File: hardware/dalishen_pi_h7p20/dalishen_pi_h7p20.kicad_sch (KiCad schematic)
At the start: 113 parts, among them J6 5V, J7 OV5640, J8 Conn_02x07_Odd_Even, J9 D500C930SV0, SW1 SW_Push, SW2 SW_Push, U3 H7P20N0L128-M3H1, U4 SY7201ABC, U5 XC6206-2.8, U7 P25Q32SH-SSH-IT, U8 XC6206-1.5, X2 XO32,26M

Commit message: [usb_sniffer_h7p20] 结构优化与验证
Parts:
- removed D7: 1N5819(S4),NC, vllogic:D_SOD-323_BAT60, symbol Device:D_Schottky
- removed J8: Conn_02x07_Odd_Even, Connector_PinHeader_1.27mm:PinHeader_2x07_P1.27mm_Vertical_SMD, symbol Connector_Generic:Conn_02x07_Odd_Even
- removed JP1: SolderJumper_3_Bridged12, Jumper:SolderJumper-3_P1.3mm_Bridged12_RoundedPad1.0x1.5mm_NumberLabels, symbol Jumper:SolderJumper_3_Bridged12
- removed JP7, JP8: SolderJumper_2_Bridged, Jumper:SolderJumper-2_P1.3mm_Bridged_RoundedPad1.0x1.5mm, symbol Jumper:SolderJumper_2_Bridged
- removed R12, R13, R59, R60, R7: 5.1k, Resistor_SMD:R_0402_1005Metric, symbol Device:R
- removed R14, R17, R6, R67, R8, R9: 0,NC, Resistor_SMD:R_0402_1005Metric, symbol Device:R
- removed R58: NC, Resistor_SMD:R_0402_1005Metric, symbol Device:R
- added J1: Conn_02x05_Odd_Even, Connector_PinHeader_1.27mm:PinHeader_2x05_P1.27mm_Vertical_SMD, symbol Connector_Generic:Conn_02x05_Odd_Even
- added JP1, JP10: SolderJumper_2_Open, Jumper:SolderJumper-2_P1.3mm_Open_RoundedPad1.0x1.5mm, symbol Jumper:SolderJumper_2_Open
- added SW3: SW_DIP_x03, Button_Switch_SMD:SW_DIP_SPSTx03_Slide_6.7x9.18mm_W8.61mm_P2.54mm_LowProfile, symbol Switch:SW_DIP_x03
- added U9: CJ3439KDW, Package_TO_SOT_SMD:SOT-363_SC-70-6, symbol vllogic_chip:CJ3439KDW
- R16: value 0,NC -> 5.1k
- R5: value 5.1k -> 10k,1%
- R56, R57: value NC -> 5.1k
- U3: footprint Package_QFP:LQFP-128_14x14mm_P0.4mm -> vllogic:LQFP-128_14x14mm_P0.4mm_pad
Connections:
- net B7_IO_20 is gone; now on net CY_SLRD: U3.24 (IO15_7)
- net B8_IO_127 is gone; now on net TP_INT: U3.127 (IO4_8)
- net B8_IO_8 is gone; now on net LED_PWM: U3.8 (IO17_8)
- net CY_FIFOADDR1 is gone; now on net B1_IO_MSEL2_125: CY_J2.8 (Pin_8)
- net CY_PA7 is gone; now on net B2_IO_CDONE_105: CY_J2.6 (Pin_6)
- net CY_SLOE is gone; now on net B1_IO_MSEL0_122: CY_J2.11 (Pin_11)
- net MSC is gone; now on net GND: U3.107 (MSC)
- net AVDD_2V8: now also J7.2 (Pin_2), J7.21 (Pin_21); no longer J7.23 (Pin_23), J7.4 (Pin_4)
- net B10_IO12N: now also J9.27 (Pin_27)
- net B10_IO12P: now also J9.28 (Pin_28)
- net B10_IO2N: now also J1.9 (Pin_9); no longer J7.18 (Pin_18)
- net B10_IO2P: now also J1.7 (Pin_7); no longer J7.16 (Pin_16)
- net B10_IO4N: now also J9.18 (Pin_18); no longer J7.14 (Pin_14)
- net B10_IO4P: now also J9.19 (Pin_19); no longer J7.12 (Pin_12)
- net B10_IO6N: now also J9.21 (Pin_21); no longer J7.22 (Pin_22)
- net B10_IO6P: now also J9.22 (Pin_22); no longer J7.20 (Pin_20)
- net B10_IO9N: now also J9.24 (Pin_24)
- net B10_IO9P: now also J9.25 (Pin_25)
- net B1_IO_MSEL0_122: now also R55.2; no longer R55.1
- net B1_IO_MSEL1_124: now also CY_J2.9 (Pin_9), R56.2; no longer R16.2, R56.1
- net B1_IO_MSEL2_125: now also R57.2; no longer R57.1
- net B2_IO_CDONE_105: now also R16.2
- net B9_IO12N: now also J7.11 (Pin_11); no longer J9.11 (Pin_11)
- net B9_IO12P: now also J7.13 (Pin_13); no longer J9.10 (Pin_10)
- net B9_IO2N: now also J9.30 (Pin_30); no longer J9.23 (Pin_23)
- net B9_IO2P: now also J9.31 (Pin_31); no longer J9.22 (Pin_22)
- net B9_IO4N: now also J1.3 (Pin_3); no longer J9.20 (Pin_20)
- net B9_IO4P: now also J1.1 (Pin_1); no longer J9.19 (Pin_19)
- net B9_IO6N: now also J7.3 (Pin_3); no longer J9.17 (Pin_17)
- net B9_IO6P: now also J7.5 (Pin_5); no longer J9.16 (Pin_16)
- net B9_IO9N: now also J7.7 (Pin_7); no longer J9.14 (Pin_14)
- net B9_IO9P: now also J7.9 (Pin_9); no longer J9.13 (Pin_13)
- net CRST_N: now also JP9.1 (A); no longer SW1.1
- net CY_SLRD: now also CY_J1.7 (Pin_7); no longer CY_J1.8 (Pin_8)
- net CY_SLWR: now also CY_J1.8 (Pin_8); no longer CY_J1.7 (Pin_7)
- net DVDD_1V5: now also J7.15 (Pin_15); no longer J7.10 (Pin_10)
- net GND: now also J7.10 (Pin_10), J7.23 (Pin_23), J9.17 (Pin_17), J9.20 (Pin_20), J9.23 (Pin_23), J9.26 (Pin_26), J9.3 (Pin_3), J9.8 (Pin_8), J1.5 (Pin_5), J1.6 (Pin_6), U9.1 (S1); no longer J7.15 (Pin_15), J7.2 (Pin_2), J9.15 (Pin_15), J9.18 (Pin_18), J9.21 (Pin_21), J9.24 (Pin_24), J9.33 (Pin_33), J9.38 (Pin_38), R5.1
- net LEDA: now also J9.34 (Pin_34), J9.35 (Pin_35); no longer J9.6 (Pin_6), J9.7 (Pin_7)
- net LEDK: now also J9.38 (Pin_38), J9.39 (Pin_39); no longer J9.2 (Pin_2), J9.3 (Pin_3)
- net OV_MCLK: now also J7.12 (Pin_12), U3.104 (IO27_GCLK_2); no longer J7.13 (Pin_13), R24.2, U3.108 (IO24_GCLK_1)
- net OV_PWDN: now also J7.17 (Pin_17), U3.102 (IO33_MISO3_2); no longer J7.8 (Pin_8), U3.101 (IO34_MISO2_2)
- net OV/TP_SCL: now also J7.20 (Pin_20), J9.4 (Pin_4), U3.101 (IO34_MISO2_2); no longer J7.5 (Pin_5), J9.37 (Pin_37), U3.106 (IO25_GCLK_2)
- net OV/TP_SDA: now also J7.22 (Pin_22), J9.5 (Pin_5), U3.99 (IO24_3); no longer J7.3 (Pin_3), J9.36 (Pin_36), U3.104 (IO27_GCLK_2)
- net TP_INT: now also J9.6 (Pin_6); no longer J9.35 (Pin_35), U3.99 (IO24_3)
- net VCCAUX: now also R5.2, U9.4 (S2); no longer C44.2, C45.2, C54.2, C56.2, C70.2, C77.2, J7.11 (Pin_11), J7.6 (Pin_6), J9.25 (Pin_25), J9.26 (Pin_26), R21.2, U3.33 (VDDIO_18), U3.35 (VDDIO_18), U3.39 (VDDIO_10), U3.48 (VDDIO_10), U3.53 (VDDIO_9), U3.62 (VDDIO_9)
- net VCC_3V3: now also J9.13 (Pin_13), J9.14 (Pin_14), J9.2 (Pin_2), J1.10 (Pin_10), J1.8 (Pin_8), SW3.1, SW3.2, SW3.3, U9.2 (G1); no longer J9.27 (Pin_27), J9.28 (Pin_28), J9.39 (Pin_39), R55.2, R56.2, R57.2
- net VCC_5V: now also J1.2 (Pin_2), J1.4 (Pin_4)
- net vllinkmodule/VL_RX: now also JP10.2 (B)
- net vllinkmodule/VL_TX: now also JP1.2 (B)
- net VDDIO_1V8: now reaches J7.19 (Pin_19)
- net VDDIO_1V8: now also C44.2, C45.2, C54.2, C56.2, C70.2, C77.2, J7.14 (Pin_14), J9.15 (Pin_15), J9.16 (Pin_16), R21.2, U3.33 (VDDIO_18), U3.35 (VDDIO_18), U3.39 (VDDIO_10), U3.48 (VDDIO_10), U3.53 (VDDIO_9), U3.62 (VDDIO_9), U9.3 (D2)
- net at R22.1: now also J9.7 (Pin_7); no longer J9.34 (Pin_34)
- net at TP1.1: now also J9.11 (Pin_11); no longer J9.30 (Pin_30)
- net at R21.1: now also J9.10 (Pin_10); no longer J9.31 (Pin_31)
- net B3_IO_102 renamed FPGA_TX
- net FPGA_TX: now also U3.106 (IO25_GCLK_2), JP10.1 (A); no longer U3.102 (IO33_MISO3_2)
- net B8_IO_126 renamed LED_PWM
- net LED_PWM: no longer U3.126 (IO3_8)
- removed net CY_FIFOADDR0: CY_J2.9 (Pin_9), R5.2
- new net: R5.1, U9.5 (G2), U9.6 (D1)
- new net: R57.1, SW3.6
- new net: R56.1, SW3.5
- new net: R55.1, SW3.4
- new net FPGA_RX: JP1.1 (A), R24.2, U3.108 (IO24_GCLK_1)
- new net KEY: SW1.1, U3.126 (IO3_8)
- no-connect marks 19 -> 18
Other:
- note added: "PD5 PD7 CLK RDY0 GND GND SCL PB0 PB2 GND"
- note added: "PD6 GND GND RDY1 VCC IFCLK SDA PB1 PB3 VCC"
- note removed: "MSC=0：配置脚3V3 MSC=1：配置脚1V8"
- note removed: "PD5 PD7 CLK RDY1 GND GND SCL PB0 PB2 GND"
- note removed: "PD6 GND GND RDY0 VCC IFCLK SDA PB1 PB3 VCC"
- moved on the sheet: C16, C44, C54, D1, D2, D3, D4, R15, R16, R18, R19, R20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

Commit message: [dalishen_pi_h7p20] backup
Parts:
- removed C3: 0.1uF, Capacitor_SMD:C_0402_1005Metric, symbol Device:C
- removed R4: 33, Resistor_SMD:R_0402_1005Metric, symbol Device:R
- removed R66: NC, Resistor_SMD:R_0402_1005Metric, symbol Device:R
- removed X2: XO32,26M, vllogic:OSC_3225, symbol Oscillator:XO32
- added C41, C80: NC, Capacitor_SMD:C_0402_1005Metric, symbol Device:C
- C4: value 10uF -> NC
- R16, R23, R24, R25, R26, R27, R28, R55, R56, R57: value 5.1k -> 2.49k
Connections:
- net GND: now also C41.1, C80.1
- net VDD_CORE: now also C41.2, C80.2
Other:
- moved on the sheet: C10, C11, C16, C17, C18, C19, C20, C21, C22, C23, C24, C38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

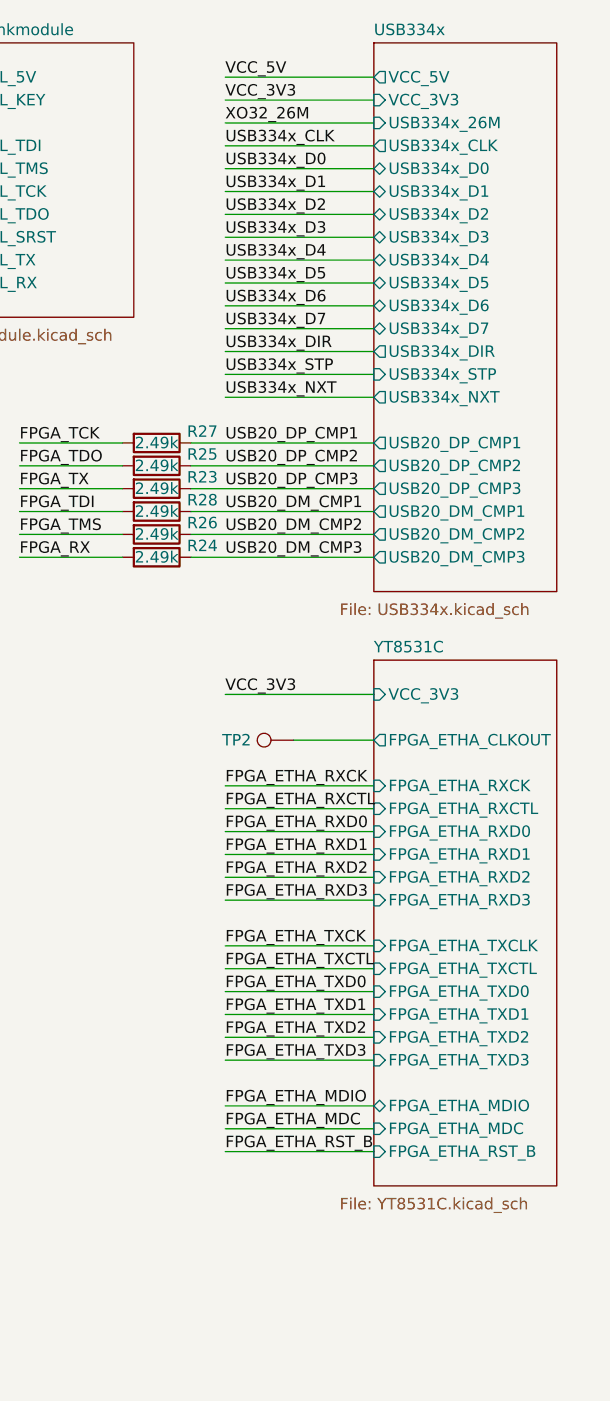
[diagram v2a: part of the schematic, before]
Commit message: [usb_sniffer_h7p20] USB3343兼容CH132F，作相关调整
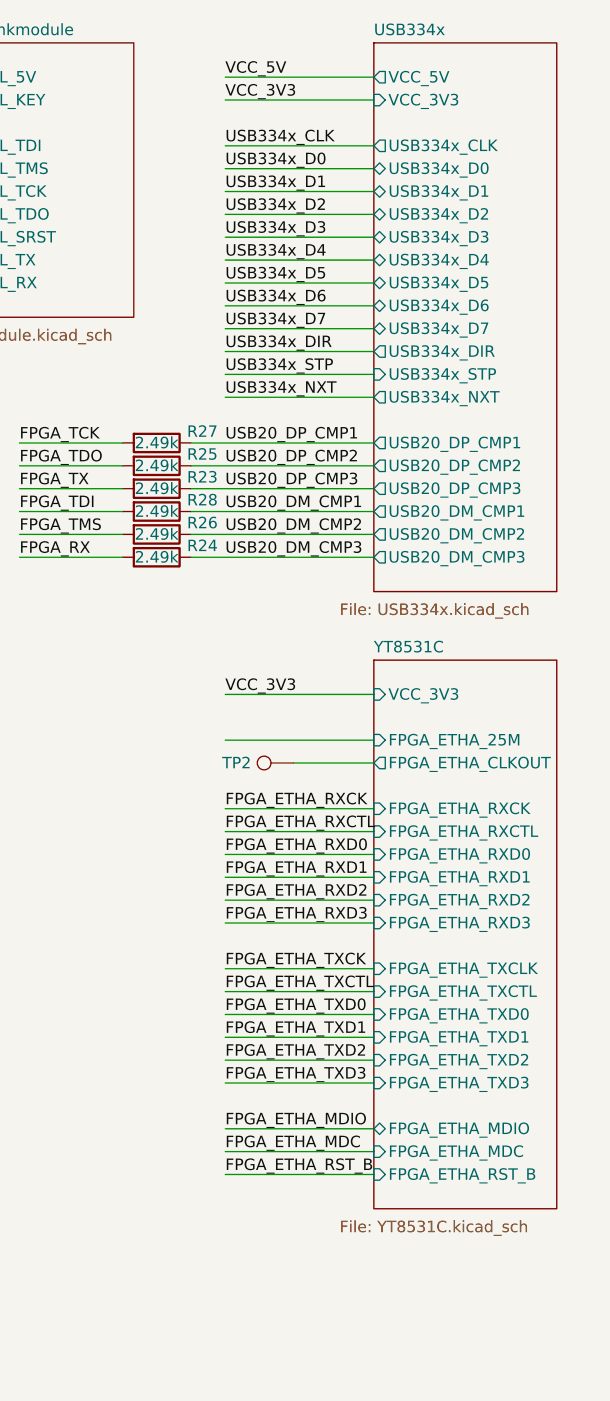
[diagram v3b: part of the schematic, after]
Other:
- sheet USB334x ports: added none; removed USB334x_26M
- sheet YT8531C ports: added FPGA_ETHA_25M; removed none
- moved on the sheet: TP2

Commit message: [dalishen_pi_h7p20] 原理图初稿
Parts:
- removed R5: 10k,1%, Resistor_SMD:R_0402_1005Metric, symbol Device:R
- removed U9: CJ3439KDW, Package_TO_SOT_SMD:SOT-363_SC-70-6, symbol vllogic_chip:CJ3439KDW
- added C2: NC, Capacitor_SMD:C_0402_1005Metric, symbol Device:C
- added R7: NC, Resistor_SMD:R_0402_1005Metric, symbol Device:R
- added R8: 33, Resistor_SMD:R_0402_1005Metric, symbol Device:R
- added X1: NC, vllogic:OSC_3225, symbol Oscillator:XO32
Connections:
- net GND: now also C2.1, X1.2 (GND)
- net VCC_3V3: now also C2.2, R7.1, X1.4 (V+)
- net at U3.6 (IO13_PCLK_8): now also R8.1
- net FPGA_ETHA_25M: now reaches U3.82 (IO3_3)
- new net: R7.2, X1.1 (EN)
- new net: R8.2, X1.3 (OUT)
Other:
- removed sheet ET3036C
- added sheet ET3036C_CJ3439KDW (ET3036C_CJ3439KDW.kicad_sch)
- moved on the sheet: C10, C11, C16, C17, C18, C19, C20, C21, C22, C23, C24, C38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

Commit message: [dalishen_pi_h7p20] 原理图预审
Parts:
- removed C80: NC, Capacitor_SMD:C_0402_1005Metric, symbol Device:C
- C69: value 1uF/35V -> 1uF,50V
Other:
- moved on the sheet: C10, C11, C16, C17, C18, C19, C2, C20, C21, C22, C23, C24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

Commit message: [dalishen_pi_h7p20] 原理图预审
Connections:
- net VCC_3V3: now also C70.2, J9.15 (Pin_15), J9.16 (Pin_16), R21.2
- net VDDIO_1V8: no longer C70.2, J9.15 (Pin_15), J9.16 (Pin_16), R21.2
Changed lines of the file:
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@@
-    (effects (font (size 1.27 1.27)) (justify left bottom))
-  )
-  (label "VDDIO_1V8" (at 374.65 240.03 0) (fields_autoplaced)
     (effects (font (size 1.27 1.27)) (justify left bottom))
   )
@@
     (effects (font (size 1.27 1.27)) (justify left bottom))
   )
-  (label "VDDIO_1V8" (at 374.65 242.57 0) (fields_autoplaced)
-    (effects (font (size 1.27 1.27)) (justify left bottom))
-  )
   (label "FPGA_RX" (at 132.08 50.8 90) (fields_autoplaced)
     (effects (font (size 1.27 1.27)) (justify left bottom))
@@
     (effects (font (size 1.27 1.27)) (justify left bottom))
   )
+  (label "VCC_3V3" (at 374.65 242.57 0) (fields_autoplaced)
+    (effects (font (size 1.27 1.27)) (justify left bottom))
+  )
   (label "FPGA_ETHA_25M" (at 367.03 93.98 0) (fields_autoplaced)
     (effects (font (size 1.27 1.27)) (justify left bottom))
@@
     (effects (font (size 1.27 1.27)) (justify left bottom))
   )
+  (label "VCC_3V3" (at 374.65 240.03 0) (fields_autoplaced)
+    (effects (font (size 1.27 1.27)) (justify left bottom))
+  )
